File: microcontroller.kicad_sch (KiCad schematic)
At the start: 20 parts

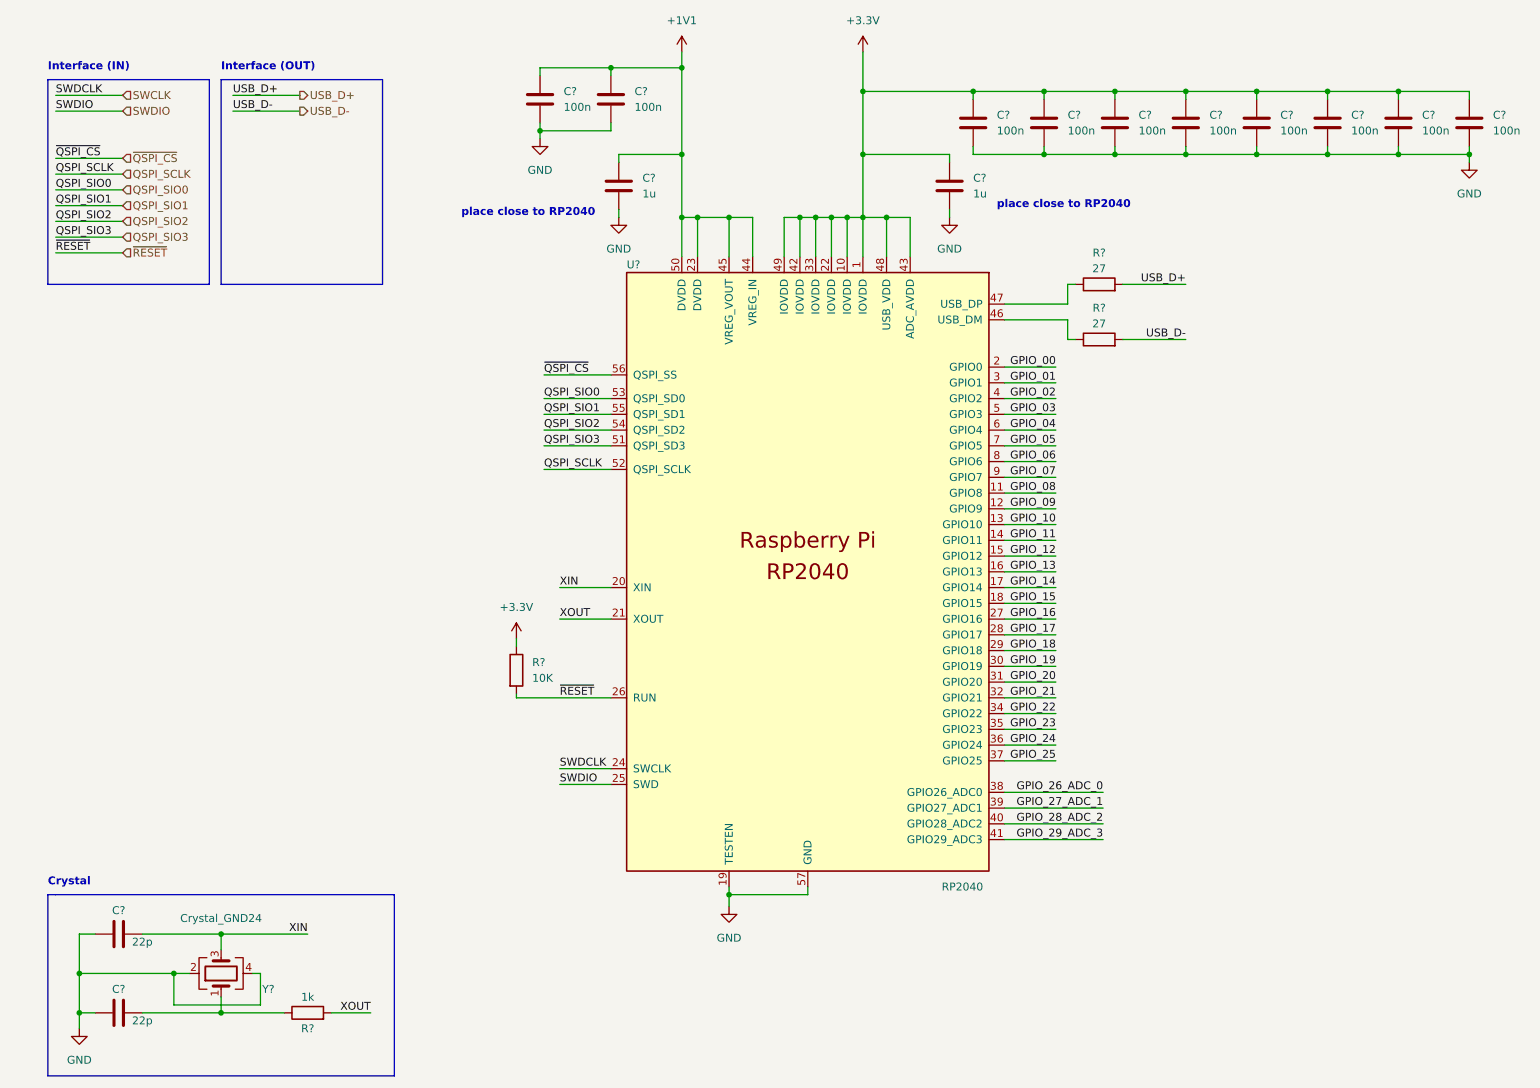
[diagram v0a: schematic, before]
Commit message: All component except led matrix
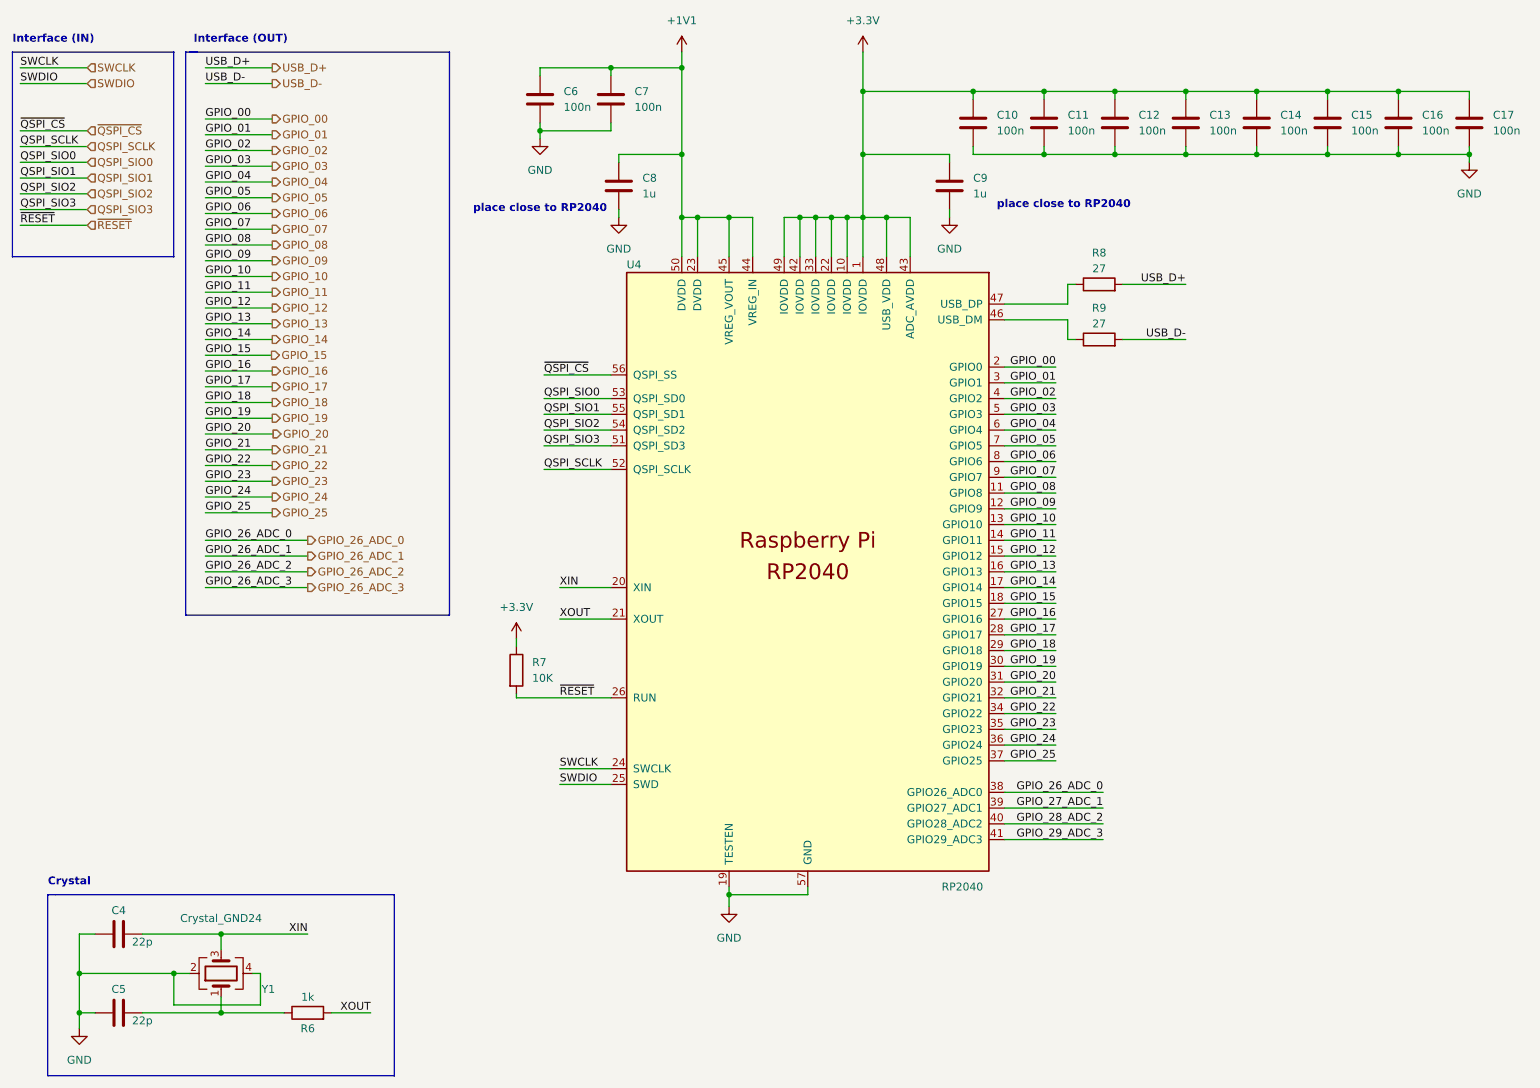
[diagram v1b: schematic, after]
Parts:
- gave numbers to parts that had none: 20

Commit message: finish schematic, prep pcb
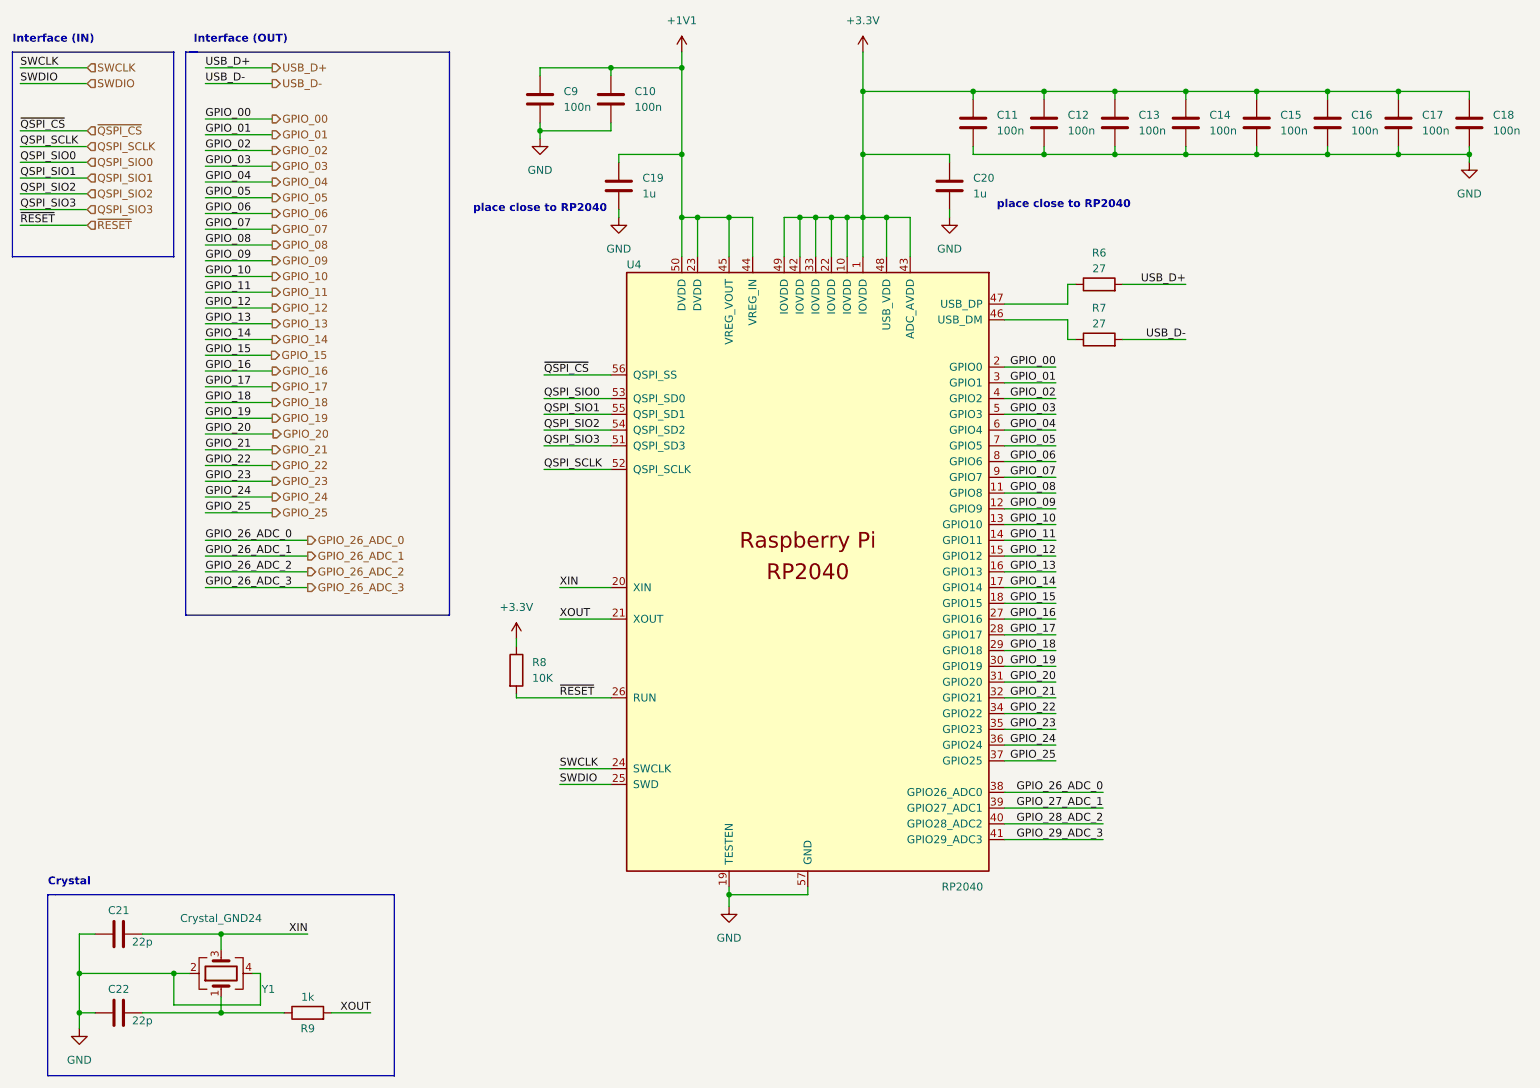
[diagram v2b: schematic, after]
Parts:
- C10: renamed from C7; footprint (none) -> Capacitor_SMD:C_0402_1005Metric
- C11: renamed from C10; footprint (none) -> Capacitor_SMD:C_0402_1005Metric
- C12: renamed from C11; footprint (none) -> Capacitor_SMD:C_0402_1005Metric
- C13: renamed from C12; footprint (none) -> Capacitor_SMD:C_0402_1005Metric
- C14: renamed from C13; footprint (none) -> Capacitor_SMD:C_0402_1005Metric
- C15: renamed from C14; footprint (none) -> Capacitor_SMD:C_0402_1005Metric
- C16: renamed from C15; footprint (none) -> Capacitor_SMD:C_0402_1005Metric
- C17: renamed from C16; footprint (none) -> Capacitor_SMD:C_0402_1005Metric
- C18: renamed from C17; footprint (none) -> Capacitor_SMD:C_0402_1005Metric
- C19: renamed from C8; footprint (none) -> Capacitor_SMD:C_0402_1005Metric
- C20: renamed from C9; footprint (none) -> Capacitor_SMD:C_0402_1005Metric
- C21: renamed from C4; footprint (none) -> Capacitor_SMD:C_0402_1005Metric
- C22: renamed from C5; footprint (none) -> Capacitor_SMD:C_0402_1005Metric
- C9: renamed from C6; footprint (none) -> Capacitor_SMD:C_0402_1005Metric
- R6: renamed from R8; footprint (none) -> Resistor_SMD:R_0603_1608Metric
- R7: renamed from R9; footprint (none) -> Resistor_SMD:R_0603_1608Metric
- R8: renamed from R7; footprint (none) -> Resistor_SMD:R_0402_1005Metric
- R9: renamed from R6; footprint (none) -> Resistor_SMD:R_0402_1005Metric
- U4: footprint RP2040_minimal:RP2040-QFN-56 -> pico-card:RP2040-QFN-56
- Y1: footprint (none) -> Crystal:Crystal_SMD_3225-4Pin_3.2x2.5mm

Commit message: Basic routing MCU, crystal, flash, crypto
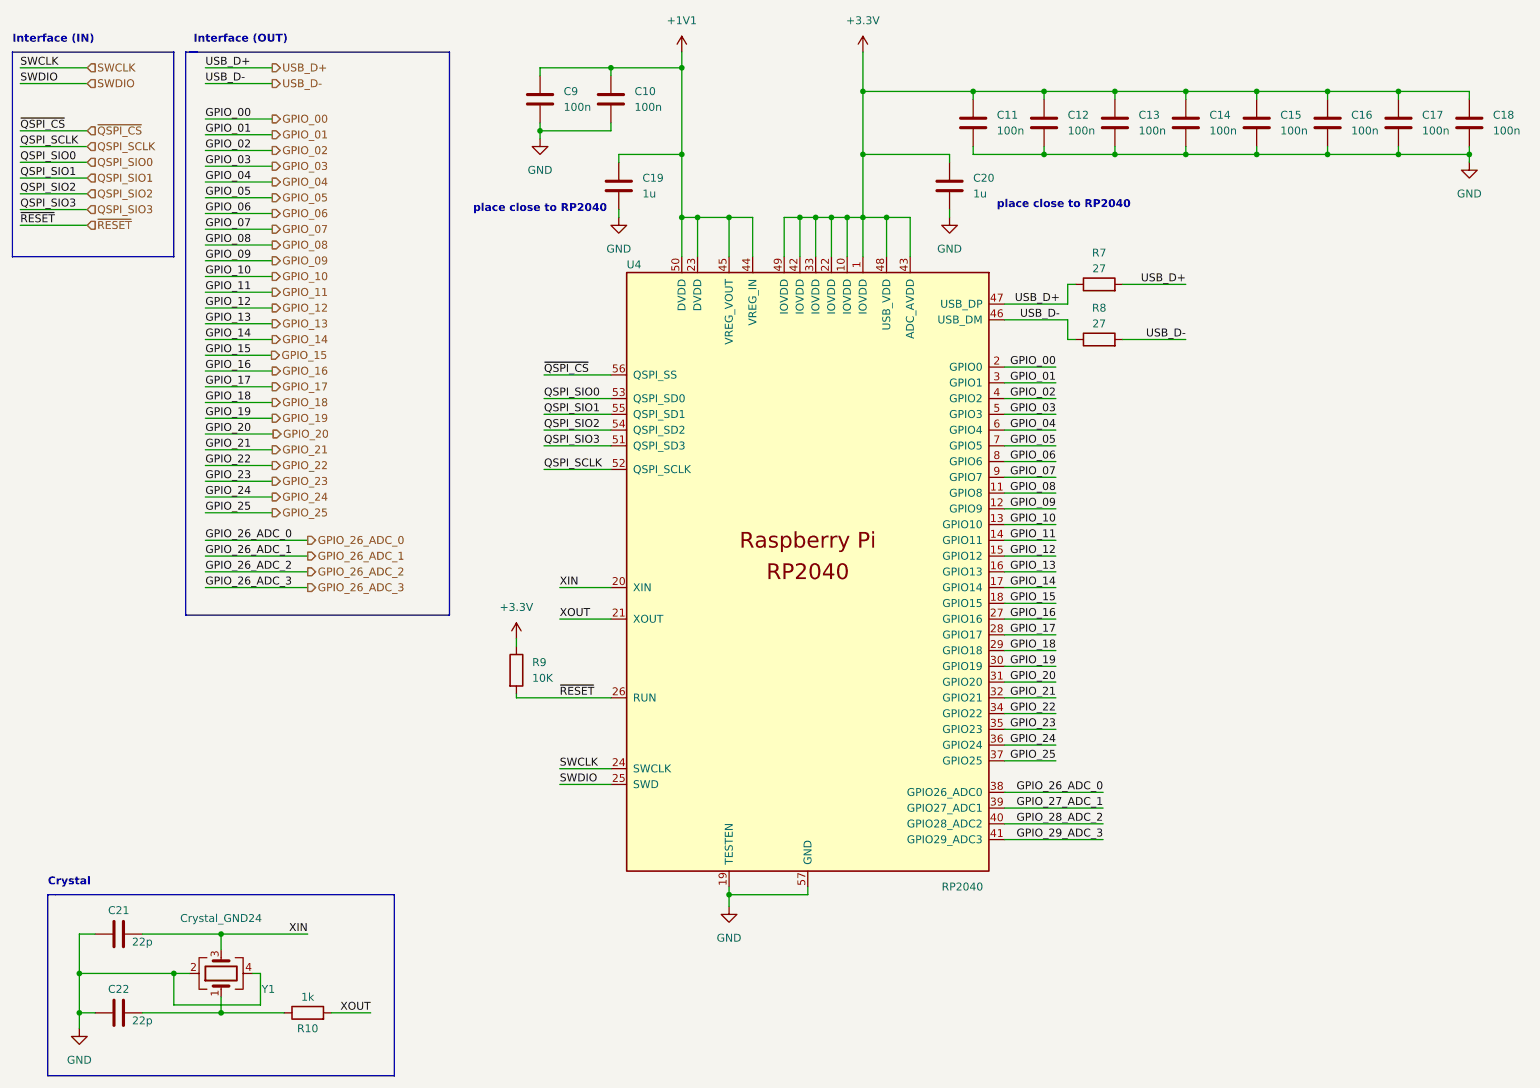
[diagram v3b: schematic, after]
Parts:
- R7: renamed from R6; footprint Resistor_SMD:R_0603_1608Metric -> Resistor_SMD:R_0402_1005Metric
- R8: renamed from R7; footprint Resistor_SMD:R_0603_1608Metric -> Resistor_SMD:R_0402_1005Metric
- renumbered R9 to R10, R8 to R9
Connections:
- net USB_D+: now also R7.1, U4.47 (USB_DP)
- net USB_D-: now also R8.1, U4.46 (USB_DM)
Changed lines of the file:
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@@
+    (effects (font (size 1.27 1.27)) (justify right bottom))
+  )
+  (label "USB_D-" (at 184.15 68.58 180)
     (effects (font (size 1.27 1.27)) (justify right bottom))
   )
@@
     (effects (font (size 1.27 1.27)) (justify left bottom))
   )
+  (label "USB_D+" (at 184.15 66.04 180)
+    (effects (font (size 1.27 1.27)) (justify right bottom))
+  )
   (label "GPIO_18" (at 183.515 121.92 180)
     (effects (font (size 1.27 1.27)) (justify right bottom))
@@
   (symbol (lib_id "power:GND") (at 113.03 52.07 0) (unit 1)
     (in_bom yes) (on_board yes) (fields_autoplaced)
-    (property "Reference" "#PWR068" (id 0) (at 113.03 58.42 0)
+    (property "Reference" "#PWR071" (id 0) (at 113.03 58.42 0)
       (effects (font (size 1.27 1.27)) hide)
     )
@@
   (symbol (lib_id "power:+3.3V") (at 96.52 120.015 0) (mirror y) (unit 1)
     (in_bom yes) (on_board yes) (fields_autoplaced)
-    (property "Reference" "#PWR070" (id 0) (at 96.52 123.825 0)
+    (property "Reference" "#PWR073" (id 0) (at 96.52 123.825 0)
       (effects (font (size 1.27 1.27)) hide)
     )
@@
   (symbol (lib_id "Device:R") (at 96.52 125.095 0) (unit 1)
     (in_bom yes) (on_board yes) (fields_autoplaced)
-    (property "Reference" "R8" (id 0) (at 99.06 123.8249 0)
+    (property "Reference" "R9" (id 0) (at 99.06 123.8249 0)
       (effects (font (size 1.27 1.27)) (justify left))
     )
@@
   (symbol (lib_id "power:GND") (at 26.035 182.88 0) (unit 1)
     (in_bom yes) (on_board yes) (fields_autoplaced)
-    (property "Reference" "#PWR072" (id 0) (at 26.035 189.23 0)
+    (property "Reference" "#PWR075" (id 0) (at 26.035 189.23 0)
       (effects (font (size 1.27 1.27)) hide)
     )
@@
   (symbol (lib_id "Device:R") (at 62.865 180.34 90) (unit 1)
     (in_bom yes) (on_board yes)
-    (property "Reference" "R9" (id 0) (at 62.865 182.88 90))
+    (property "Reference" "R10" (id 0) (at 62.865 182.88 90))
     (property "Value" "1k" (id 1) (at 62.865 177.8 90))
     (property "Footprint" "Resistor_SMD:R_0402_1005Metric" (id 2) (at 62.865 182.118 90)
@@
   (symbol (lib_id "power:GND") (at 250.19 43.18 0) (unit 1)
     (in_bom yes) (on_board yes) (fields_autoplaced)
-    (property "Reference" "#PWR067" (id 0) (at 250.19 49.53 0)
+    (property "Reference" "#PWR070" (id 0) (at 250.19 49.53 0)
       (effects (font (size 1.27 1.27)) hide)
     )
@@
   (symbol (lib_id "Device:R") (at 190.5 71.755 90) (unit 1)
     (in_bom yes) (on_board yes)
-    (property "Reference" "R7" (id 0) (at 190.5 66.675 90))
+    (property "Reference" "R8" (id 0) (at 190.5 66.675 90))
     (property "Value" "27" (id 1) (at 190.5 69.215 90))
-    (property "Footprint" "Resistor_SMD:R_0603_1608Metric" (id 2) (at 190.5 73.533 90)
+    (property "Footprint" "Resistor_SMD:R_0402_1005Metric" (id 2) (at 190.5 73.533 90)
       (effects (font (size 1.27 1.27)) hide)
     )
@@
   (symbol (lib_id "power:+3.3V") (at 152.4 25.4 0) (mirror y) (unit 1)
     (in_bom yes) (on_board yes) (fields_autoplaced)
-    (property "Reference" "#PWR065" (id 0) (at 152.4 29.21 0)
+    (property "Reference" "#PWR068" (id 0) (at 152.4 29.21 0)
       (effects (font (size 1.27 1.27)) hide)
     )
@@
   (symbol (lib_id "power:GND") (at 100.33 39.37 0) (unit 1)
     (in_bom yes) (on_board yes) (fields_autoplaced)
-    (property "Reference" "#PWR066" (id 0) (at 100.33 45.72 0)
+    (property "Reference" "#PWR069" (id 0) (at 100.33 45.72 0)
       (effects (font (size 1.27 1.27)) hide)
     )
@@
   (symbol (lib_id "power:GND") (at 130.81 163.195 0) (unit 1)
     (in_bom yes) (on_board yes) (fields_autoplaced)
-    (property "Reference" "#PWR071" (id 0) (at 130.81 169.545 0)
+    (property "Reference" "#PWR074" (id 0) (at 130.81 169.545 0)
       (effects (font (size 1.27 1.27)) hide)
     )
@@
   (symbol (lib_id "Device:R") (at 190.5 62.865 90) (unit 1)
     (in_bom yes) (on_board yes)
-    (property "Reference" "R6" (id 0) (at 190.5 57.785 90))
+    (property "Reference" "R7" (id 0) (at 190.5 57.785 90))
     (property "Value" "27" (id 1) (at 190.5 60.325 90))
-    (property "Footprint" "Resistor_SMD:R_0603_1608Metric" (id 2) (at 190.5 64.643 90)
+    (property "Footprint" "Resistor_SMD:R_0402_1005Metric" (id 2) (at 190.5 64.643 90)
       (effects (font (size 1.27 1.27)) hide)
     )
@@
   (symbol (lib_id "power:GND") (at 166.37 52.07 0) (unit 1)
     (in_bom yes) (on_board yes) (fields_autoplaced)
-    (property "Reference" "#PWR069" (id 0) (at 166.37 58.42 0)
+    (property "Reference" "#PWR072" (id 0) (at 166.37 58.42 0)
       (effects (font (size 1.27 1.27)) hide)
     )
@@
   (symbol (lib_id "power:+1V1") (at 123.19 25.4 0) (unit 1)
     (in_bom yes) (on_board yes) (fields_autoplaced)
-    (property "Reference" "#PWR064" (id 0) (at 123.19 29.21 0)
-      (effects (font (size 1.27 1.27)) hide)
-    )
+    (property "Reference" "#PWR067" (id 0) (at 123.19 29.21 0)
+      (effects (font (size 1.27 1.27)) hide)
+    )
